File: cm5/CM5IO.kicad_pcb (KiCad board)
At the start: 4 copper layers, 101.9 x 90.8 mm, 71 parts, among them J1 67910-5700, J14 JST_SHBM04B-SRSS-TB, J2 B2B-XH-A_LF__SN_, J4 0786463001, J5 USB3_A, J6 Conn_02x03_Counter_Clockwise, J7 Conn_01x04, U1 CAT24C128, U2 TLV320ADC6120IRTER, U5 74LVC1G07SE-7, U6 AP22653W6, U8 AP3441SHE-7B

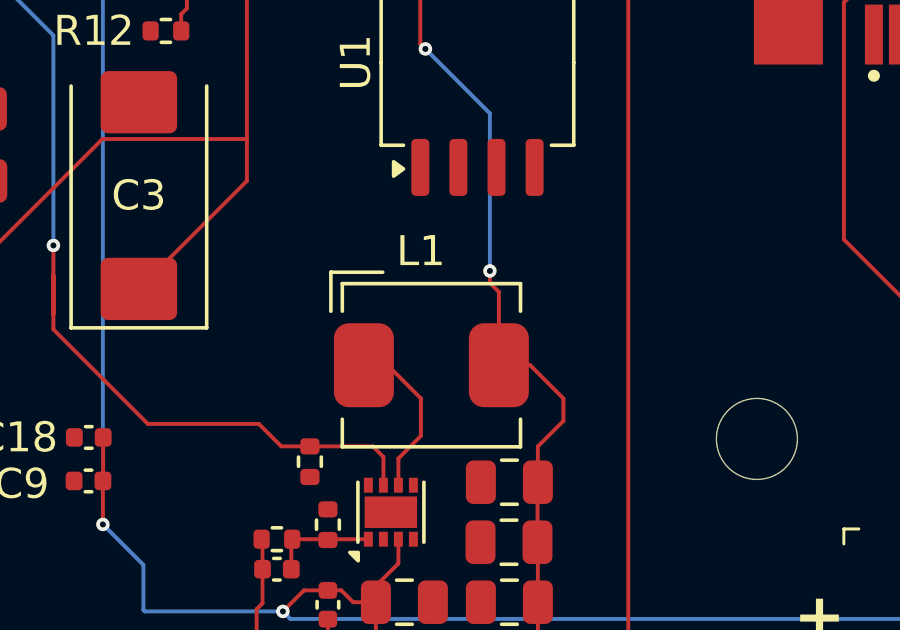
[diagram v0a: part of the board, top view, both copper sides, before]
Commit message: Hopefully these are the corrected parts, need to cross-reference the BOM to what was ordered
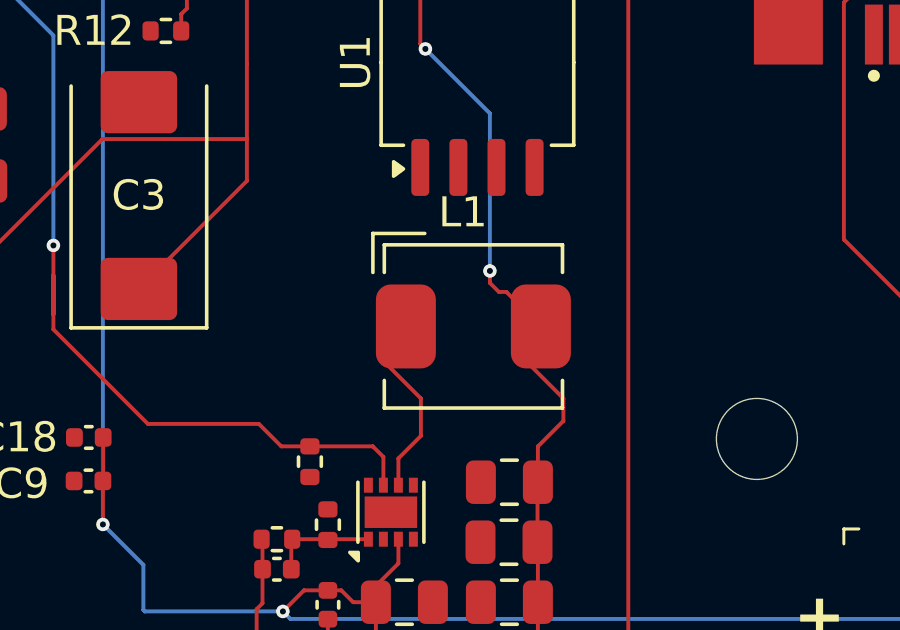
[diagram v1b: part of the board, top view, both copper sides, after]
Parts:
- moved L1 1.91 mm to (197.1, 145.9)
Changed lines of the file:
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@@
 			)
 		)
-		(property "LCSC" "C2297"
+		(property "LCSC" "C12624"
 			(at 0 0 0)
 			(layer "F.SilkS")
@@
 			)
 		)
-		(property "LCSC" "C327024"
+		(property "LCSC" "C1525"
 			(at 0 0 0)
 			(layer "F.SilkS")
@@
 			)
 		)
-		(property "LCSC" "C327024"
+		(property "LCSC" "C1525"
 			(at 0 0 0)
 			(layer "F.SilkS")
@@
 			)
 		)
-		(property "LCSC" "C327024"
+		(property "LCSC" "C1525"
 			(at 0 0 0)
 			(layer "F.SilkS")
@@
 	(footprint "CM5IO:L_Bourns_SRP5030CC"
 		(layer "F.Cu")
-		(at 195.65 147.2425)
+		(at 197.05 145.95)
 		(descr "Inductor, Bourns, SRP5030T, 5.7mmx5.2mm (Script generated with StandardBox.py) (https://www.bourns.com/data/global/pdfs/SRP5030T.pdf)")
 		(tags "Inductor Bourns_SRP5030T")
@@
 			)
 		)
+		(property "LCSC" "C22404330"
+			(at 0 0 0)
+			(layer "F.SilkS")
+			(hide yes)
+			(effects
+				(font
+					(size 1.27 1.27)
+					(thickness 0.15)
+				)
+			)
+		)
 		(property ki_fp_filters "Choke_* *Coil* Inductor_* L_*")
 		(sheetname "/PCIe-M2/")
@@
 			)
 		)
-		(property "LCSC" "C327024"
+		(property "LCSC" "C1525"
 			(at 0 0 0)
 			(layer "F.SilkS")
@@
 			)
 		)
-		(property "LCSC" "C327024"
+		(property "LCSC" "C1525"
 			(at 0 0 0)
 			(layer "F.SilkS")
@@
 			)
 		)
-		(property "LCSC" "C327024"
+		(property "LCSC" "C1525"
 			(at 0 0 0)
 			(layer "F.SilkS")
@@
 			)
 		)
-		(property "LCSC" "C327024"
+		(property "LCSC" "C1525"
 			(at 0 0 90)
 			(layer "F.SilkS")
@@
 			)
 		)
-		(property "LCSC" "C327024"
+		(property "LCSC" "C1525"
 			(at 0 0 0)
 			(layer "F.SilkS")
@@
 	)
 	(segment
-		(start 190.02 155.18)
-		(end 190.02 154.0425)
+		(start 197.6 144.1)
+		(end 197.6 144.5)
 		(width 0.13)
 		(layer "F.Cu")
@@
 	)
 	(segment
-		(start 200.05 149.1)
-		(end 200.05 148.35)
+		(start 199.2 151.1425)
+		(end 199.2 149.95)
+		(width 0.13)
+		(layer "F.Cu")
+		(net 6)
+	)
+	(segment
+		(start 190.02 155.18)
+		(end 190.02 154.0425)
 		(width 0.13)
 		(layer "F.Cu")
@@
 	)
 	(segment
-		(start 197.9 144.8)
-		(end 197.9 147.2425)
+		(start 200.05 149.1)
+		(end 200.05 148.35)
 		(width 0.13)
 		(layer "F.Cu")
@@
 	)
 	(segment
-		(start 197.6 144.1)
-		(end 197.6 144.5)
-		(width 0.13)
-		(layer "F.Cu")
-		(net 6)
-	)
-	(segment
-		(start 198.9425 147.2425)
-		(end 197.9 147.2425)
-		(width 0.13)
-		(layer "F.Cu")
-		(net 6)
-	)
-	(segment
-		(start 199.2 151.1425)
-		(end 199.2 149.95)
-		(width 0.13)
-		(layer "F.Cu")
-		(net 6)
-	)
-	(segment
 		(start 199.2 157.1425)
 		(end 199.2 158.05)
@@
 	)
 	(segment
-		(start 200.05 148.35)
-		(end 198.9425 147.2425)
+		(start 228.8875 133.4375)
+		(end 226.95 131.5)
 		(width 0.13)
 		(layer "F.Cu")
@@
 	)
 	(segment
-		(start 228.8875 133.4375)
-		(end 226.95 131.5)
+		(start 199.2 149.95)
+		(end 200.05 149.1)
 		(width 0.13)
 		(layer "F.Cu")
@@
 	)
 	(segment
-		(start 199.2 149.95)
-		(end 200.05 149.1)
-		(width 0.13)
-		(layer "F.Cu")
-		(net 6)
-	)
-	(segment
 		(start 195.28 133.65)
 		(end 195.28 136.53)
@@
 	)
 	(segment
+		(start 197.9 144.8)
+		(end 198.15 144.8)
+		(width 0.13)
+		(layer "F.Cu")
+		(net 6)
+	)
+	(segment
 		(start 195.28 136.53)
 		(end 195.45 136.7)
@@
 	)
 	(segment
+		(start 197.6 144.5)
+		(end 197.9 144.8)
+		(width 0.13)
+		(layer "F.Cu")
+		(net 6)
+	)
+	(segment
 		(start 202.45 126.95)
 		(end 202.4 127)
@@
 	)
 	(segment
+		(start 198.9425 147.2425)
+		(end 198.9425 146.3075)
+		(width 0.13)
+		(layer "F.Cu")
+		(net 6)
+	)
+	(segment
 		(start 189.825 157)
 		(end 189.825 155.375)
@@
 	)
 	(segment
-		(start 197.6 144.5)
-		(end 197.9 144.8)
+		(start 198.9425 146.3075)
+		(end 199.3 145.95)
 		(width 0.13)
 		(layer "F.Cu")
@@
 		(width 0.13)
 		(layer "F.Cu")
+		(net 6)
+	)
+	(segment
+		(start 200.05 148.35)
+		(end 198.9425 147.2425)
+		(width 0.13)
+		(layer "F.Cu")
+		(net 6)
+	)
+	(segment
+		(start 198.15 144.8)
+		(end 199.3 145.95)
+		(width 0.13)
+		(layer "F.Cu")

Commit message: Uh in this version, I have made the 5v trace fatter
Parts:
- removed C23: 100n, Capacitor_SMD:C_0402_1005Metric
- removed D4: LED Red, LED_SMD:LED_0603_1608Metric
- removed R11: 330, Resistor_SMD:R_0603_1608Metric
- removed U1: CAT24C128, Package_SO:SOIC-8_5.3x6.2mm_P1.27mm
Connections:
- J1 pad 11: /CM5_GPIO ( Ethernet, GPIO, SDCARD)/GPIO14 -> unconnected-(J1-Pad11)
- J1 pad 13: /CM5_GPIO ( Ethernet, GPIO, SDCARD)/GPIO15 -> unconnected-(J1-Pad13)
- J1 pad 31: /CM5_GPIO ( Ethernet, GPIO, SDCARD)/GPIO13 -> /PCIe-M2/DTR
- R14 pad 1: /CM5_HighSpeed/PCIE_PWR_EN -> /PCIe-M2/PCIE_PWR_EN
- U2 pad 22: GND -> (no net)
- U2 pad 23: GND -> (no net)
- U2 pad 24: GND -> (no net)
- U2 pad 25: GND -> (no net)
- U8 pad 7: /CM5_HighSpeed/PCIE_PWR_EN -> /PCIe-M2/PCIE_PWR_EN
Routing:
- net /CM5_GPIO ( Ethernet, GPIO, SDCARD)/GPIO14: track 60.2 -> 0.00 mm, vias 2 -> 0
- net Net-(D4-A): track 18.0 -> 0.00 mm
- net /+5v: track 123.4 -> 132.8 mm, vias 3 -> 7
- net GND: track 113.2 -> 116.1 mm
- net /CM5_GPIO ( Ethernet, GPIO, SDCARD)/GPIO15: track 52.8 -> 50.1 mm, vias 2 -> 1
- net /CM5_GPIO ( Ethernet, GPIO, SDCARD)/GPIO13: track 54.8 -> 52.3 mm, vias 2 -> 1
- net /CM5_HighSpeed/USB3-1-TX_N: track 68.0 -> 66.3 mm
- net /+3.3v: track 161.0 -> 161.7 mm
- added copper zone on F.Cu, net /+5v
